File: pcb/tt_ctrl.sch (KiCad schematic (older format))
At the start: 14 parts

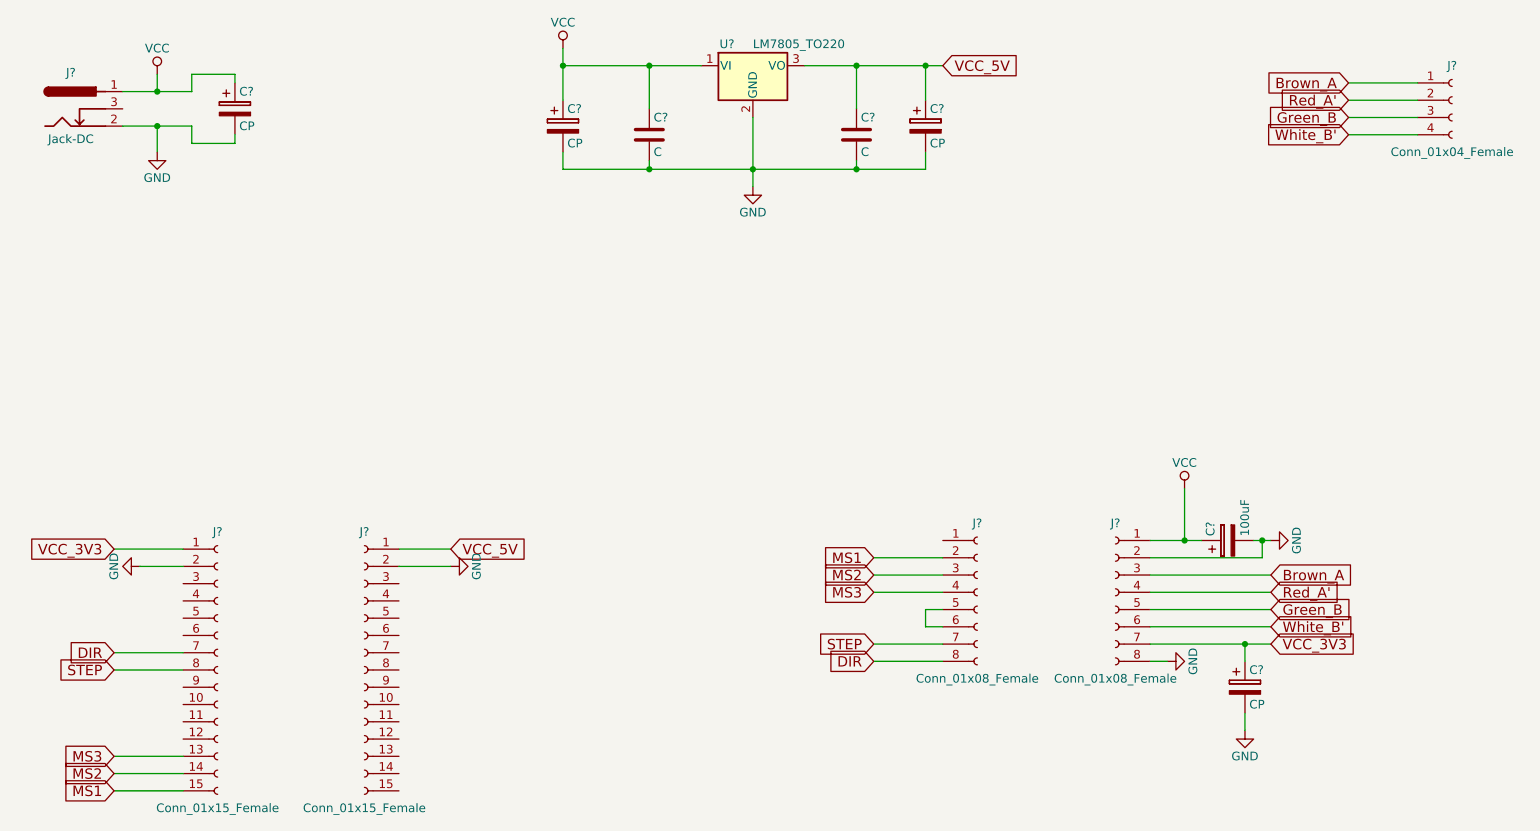
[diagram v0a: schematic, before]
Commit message: First version of the PCB added.
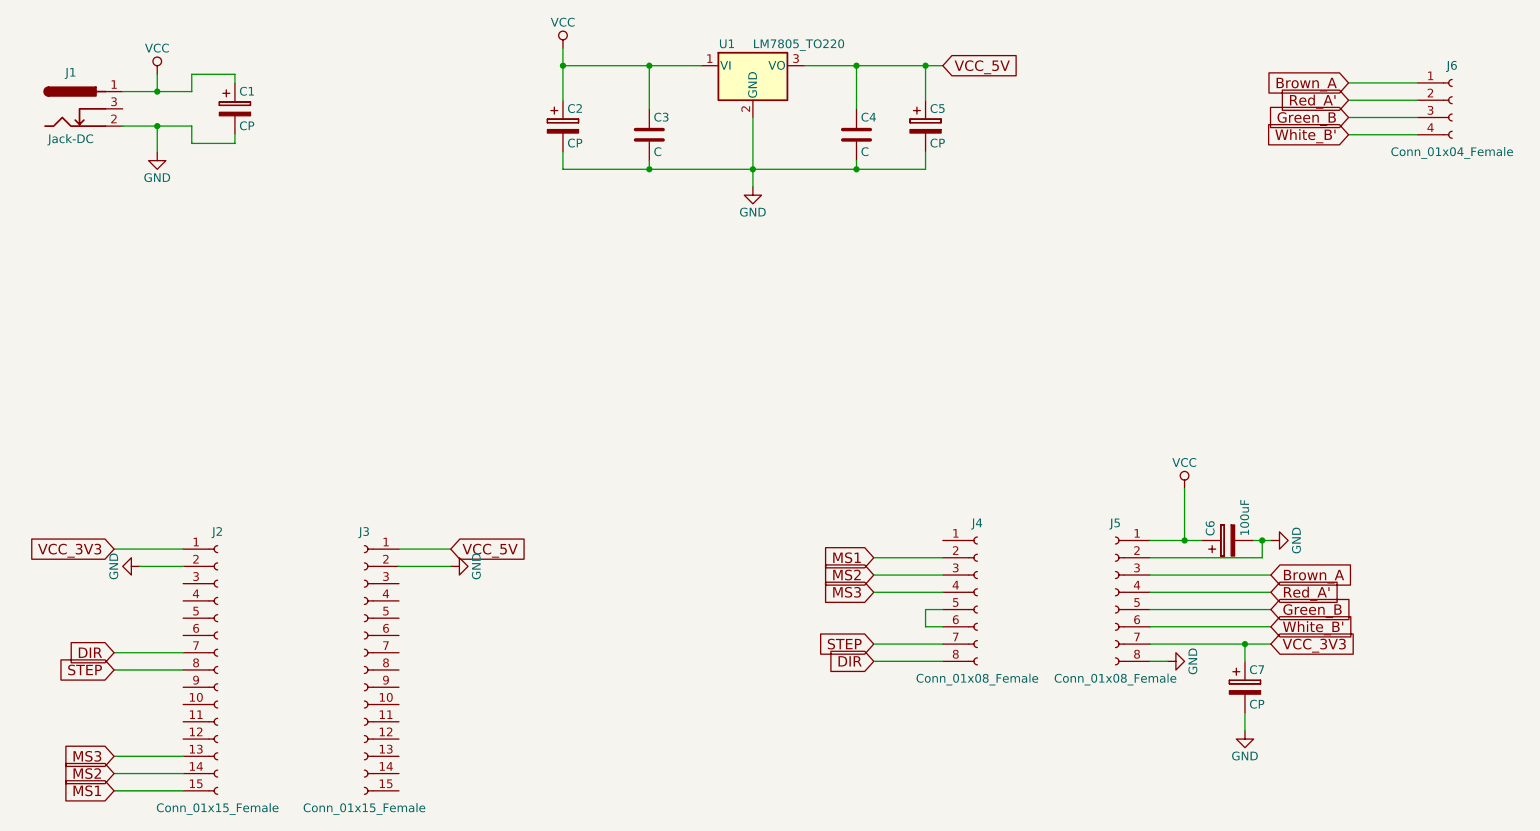
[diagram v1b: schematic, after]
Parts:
- C1, C2, C5, C6, C7: renamed from C?; footprint (none) -> Capacitors_THT:CP_Radial_D5.0mm_P2.50mm
- C3, C4: renamed from C?; footprint (none) -> Capacitors_THT:C_Disc_D5.0mm_W2.5mm_P2.50mm
- J1: renamed from J?; footprint (none) -> Connectors:BARREL_JACK
- J2, J3: renamed from J?; footprint (none) -> Socket_Strips:Socket_Strip_Straight_1x15_Pitch2.54mm
- J4, J5: renamed from J?; footprint (none) -> Socket_Strips:Socket_Strip_Straight_1x08_Pitch2.54mm
- J6: renamed from J?; footprint (none) -> Socket_Strips:Socket_Strip_Straight_1x04_Pitch2.54mm
- U1: renamed from U?; footprint TO_SOT_Packages_THT:TO-220_Vertical -> Power_Integrations:TO-220
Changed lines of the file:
@@
 LIBS:contrib
 LIBS:valves
+LIBS:tt_ctrl-cache
 EELAYER 25 0
 EELAYER END
@@
 $EndDescr
 $Comp
-L Jack-DC J?
+L Jack-DC J1
 U 1 1 5AFD7EE6
 P 2050 2000
-F 0 "J?" H 2050 2210 50  0000 C CNN
+F 0 "J1" H 2050 2210 50  0000 C CNN
 F 1 "Jack-DC" H 2050 1825 50  0000 C CNN
-F 2 "" H 2100 1960 50  0001 C CNN
+F 2 "Connectors:BARREL_JACK" H 2100 1960 50  0001 C CNN
 F 3 "" H 2100 1960 50  0001 C CNN
 	1    2050 2000
@@
 $EndComp
 $Comp
-L GND #PWR?
+L GND #PWR01
 U 1 1 5AFD7F7B
 P 2550 2250
-F 0 "#PWR?" H 2550 2000 50  0001 C CNN
+F 0 "#PWR01" H 2550 2000 50  0001 C CNN
 F 1 "GND" H 2550 2100 50  0000 C CNN
 F 2 "" H 2550 2250 50  0001 C CNN
@@
 $EndComp
 $Comp
-L VCC #PWR?
+L VCC #PWR02
 U 1 1 5AFD7F98
 P 2550 1800
-F 0 "#PWR?" H 2550 1650 50  0001 C CNN
+F 0 "#PWR02" H 2550 1650 50  0001 C CNN
 F 1 "VCC" H 2550 1950 50  0000 C CNN
 F 2 "" H 2550 1800 50  0001 C CNN
@@
 $EndComp
 $Comp
-L Conn_01x08_Female J?
+L Conn_01x08_Female J4
 U 1 1 5AFD7FB4
 P 7300 4800
-F 0 "J?" H 7300 5200 50  0000 C CNN
+F 0 "J4" H 7300 5200 50  0000 C CNN
 F 1 "Conn_01x08_Female" H 7300 4300 50  0000 C CNN
-F 2 "" H 7300 4800 50  0001 C CNN
+F 2 "Socket_Strips:Socket_Strip_Straight_1x08_Pitch2.54mm" H 7300 4800 50  0001 C CNN
 F 3 "" H 7300 4800 50  0001 C CNN
 	1    7300 4800
@@
 $EndComp
 $Comp
-L Conn_01x08_Female J?
+L Conn_01x08_Female J5
 U 1 1 5AFD8243
 P 8100 4800
-F 0 "J?" H 8100 5200 50  0000 C CNN
+F 0 "J5" H 8100 5200 50  0000 C CNN
 F 1 "Conn_01x08_Female" H 8100 4300 50  0000 C CNN
-F 2 "" H 8100 4800 50  0001 C CNN
+F 2 "Socket_Strips:Socket_Strip_Straight_1x08_Pitch2.54mm" H 8100 4800 50  0001 C CNN
 F 3 "" H 8100 4800 50  0001 C CNN
 	1    8100 4800
@@
 $EndComp
 $Comp
-L Conn_01x15_Female J?
+L Conn_01x15_Female J2
 U 1 1 5AFD8298
 P 2900 5250
-F 0 "J?" H 2900 6050 50  0000 C CNN
+F 0 "J2" H 2900 6050 50  0000 C CNN
 F 1 "Conn_01x15_Female" H 2900 4450 50  0000 C CNN
-F 2 "" H 2900 5250 50  0001 C CNN
+F 2 "Socket_Strips:Socket_Strip_Straight_1x15_Pitch2.54mm" H 2900 5250 50  0001 C CNN
 F 3 "" H 2900 5250 50  0001 C CNN
 	1    2900 5250
@@
 $EndComp
 $Comp
-L Conn_01x15_Female J?
+L Conn_01x15_Female J3
 U 1 1 5AFD837D
 P 3750 5250
-F 0 "J?" H 3750 6050 50  0000 C CNN
+F 0 "J3" H 3750 6050 50  0000 C CNN
 F 1 "Conn_01x15_Female" H 3750 4450 50  0000 C CNN
-F 2 "" H 3750 5250 50  0001 C CNN
+F 2 "Socket_Strips:Socket_Strip_Straight_1x15_Pitch2.54mm" H 3750 5250 50  0001 C CNN
 F 3 "" H 3750 5250 50  0001 C CNN
 	1    3750 5250
@@
 $EndComp
 $Comp
-L LM7805_TO220 U?
+L LM7805_TO220 U1
 U 1 1 5AFD841A
 P 6000 1750
-F 0 "U?" H 5850 1875 50  0000 C CNN
+F 0 "U1" H 5850 1875 50  0000 C CNN
 F 1 "LM7805_TO220" H 6000 1875 50  0000 L CNN
-F 2 "TO_SOT_Packages_THT:TO-220_Vertical" H 6000 1975 50  0001 C CIN
+F 2 "Power_Integrations:TO-220" H 6000 1975 50  0001 C CIN
 F 3 "" H 6000 1700 50  0001 C CNN
 	1    6000 1750
@@
 $EndComp
 $Comp
-L C C?
+L C C3
 U 1 1 5AFD84C3
 P 5400 2150
-F 0 "C?" H 5425 2250 50  0000 L CNN
+F 0 "C3" H 5425 2250 50  0000 L CNN
 F 1 "C" H 5425 2050 50  0000 L CNN
-F 2 "" H 5438 2000 50  0001 C CNN
+F 2 "Capacitors_THT:C_Disc_D5.0mm_W2.5mm_P2.50mm" H 5438 2000 50  0001 C CNN
 F 3 "" H 5400 2150 50  0001 C CNN
 	1    5400 2150
@@
 $EndComp
 $Comp
-L C C?
+L C C4
 U 1 1 5AFD85A1
 P 6600 2150
-F 0 "C?" H 6625 2250 50  0000 L CNN
+F 0 "C4" H 6625 2250 50  0000 L CNN
 F 1 "C" H 6625 2050 50  0000 L CNN
-F 2 "" H 6638 2000 50  0001 C CNN
+F 2 "Capacitors_THT:C_Disc_D5.0mm_W2.5mm_P2.50mm" H 6638 2000 50  0001 C CNN
 F 3 "" H 6600 2150 50  0001 C CNN
 	1    6600 2150
@@
 $EndComp
 $Comp
-L CP C?
+L CP C1
 U 1 1 5AFD878C
 P 3000 2000
-F 0 "C?" H 3025 2100 50  0000 L CNN
+F 0 "C1" H 3025 2100 50  0000 L CNN
 F 1 "CP" H 3025 1900 50  0000 L CNN
-F 2 "" H 3038 1850 50  0001 C CNN
+F 2 "Capacitors_THT:CP_Radial_D5.0mm_P2.50mm" H 3038 1850 50  0001 C CNN
 F 3 "" H 3000 2000 50  0001 C CNN
 	1    3000 2000
@@
 $EndComp
 $Comp
-L CP C?
+L CP C5
 U 1 1 5AFD886B
 P 7000 2100
-F 0 "C?" H 7025 2200 50  0000 L CNN
+F 0 "C5" H 7025 2200 50  0000 L CNN
 F 1 "CP" H 7025 2000 50  0000 L CNN
-F 2 "" H 7038 1950 50  0001 C CNN
+F 2 "Capacitors_THT:CP_Radial_D5.0mm_P2.50mm" H 7038 1950 50  0001 C CNN
 F 3 "" H 7000 2100 50  0001 C CNN
 	1    7000 2100
@@
 $EndComp
 $Comp
-L CP C?
+L CP C6
 U 1 1 5AFD89BB
 P 8750 4500
-F 0 "C?" H 8775 4600 50  0000 L CNN
+F 0 "C6" H 8775 4600 50  0000 L CNN
 F 1 "100uF" H 8775 4400 50  0000 L CNN
-F 2 "" H 8788 4350 50  0001 C CNN
+F 2 "Capacitors_THT:CP_Radial_D5.0mm_P2.50mm" H 8788 4350 50  0001 C CNN
 F 3 "" H 8750 4500 50  0001 C CNN
 	1    8750 4500
@@
 $EndComp
 $Comp
-L GND #PWR?
+L GND #PWR03
 U 1 1 5AFD8D7F
 P 6000 2450
-F 0 "#PWR?" H 6000 2200 50  0001 C CNN
+F 0 "#PWR03" H 6000 2200 50  0001 C CNN
 F 1 "GND" H 6000 2300 50  0000 C CNN
 F 2 "" H 6000 2450 50  0001 C CNN
@@
 $EndComp
 $Comp
-L CP C?
+L CP C2
 U 1 1 5AFD8DA6
 P 4900 2100
-F 0 "C?" H 4925 2200 50  0000 L CNN
+F 0 "C2" H 4925 2200 50  0000 L CNN
 F 1 "CP" H 4925 2000 50  0000 L CNN
-F 2 "" H 4938 1950 50  0001 C CNN
+F 2 "Capacitors_THT:CP_Radial_D5.0mm_P2.50mm" H 4938 1950 50  0001 C CNN
 F 3 "" H 4900 2100 50  0001 C CNN
 	1    4900 2100
@@
 $EndComp
 $Comp
-L Conn_01x04_Female J?
+L Conn_01x04_Female J6
 U 1 1 5AFD8E73
 P 10050 1950
-F 0 "J?" H 10050 2150 50  0000 C CNN
+F 0 "J6" H 10050 2150 50  0000 C CNN
 F 1 "Conn_01x04_Female" H 10050 1650 50  0000 C CNN
-F 2 "" H 10050 1950 50  0001 C CNN
+F 2 "Socket_Strips:Socket_Strip_Straight_1x04_Pitch2.54mm" H 10050 1950 50  0001 C CNN
 F 3 "" H 10050 1950 50  0001 C CNN
 	1    10050 1950
@@
 $EndComp
 $Comp
-L VCC #PWR?
+L VCC #PWR04
 U 1 1 5AFD947A
 P 4900 1650
-F 0 "#PWR?" H 4900 1500 50  0001 C CNN
+F 0 "#PWR04" H 4900 1500 50  0001 C CNN
 F 1 "VCC" H 4900 1800 50  0000 C CNN
 F 2 "" H 4900 1650 50  0001 C CNN
@@
 $EndComp
 $Comp
-L GND #PWR?
+L GND #PWR05
 U 1 1 5AFD97A2
 P 8850 5600
-F 0 "#PWR?" H 8850 5350 50  0001 C CNN
+F 0 "#PWR05" H 8850 5350 50  0001 C CNN
 F 1 "GND" H 8850 5450 50  0000 C CNN
 F 2 "" H 8850 5600 50  0001 C CNN
@@
 VCC_5V
 $Comp
-L GND #PWR?
+L GND #PWR06
 U 1 1 5AFD9FFE
 P 9000 4500
-F 0 "#PWR?" H 9000 4250 50  0001 C CNN
+F 0 "#PWR06" H 9000 4250 50  0001 C CNN
 F 1 "GND" H 9000 4350 50  0000 C CNN
 F 2 "" H 9000 4500 50  0001 C CNN
@@
 White_B'
 $Comp
-L VCC #PWR?
+L VCC #PWR07
 U 1 1 5AFDAC35
 P 8500 4200
-F 0 "#PWR?" H 8500 4050 50  0001 C CNN
+F 0 "#PWR07" H 8500 4050 50  0001 C CNN
 F 1 "VCC" H 8500 4350 50  0000 C CNN
 F 2 "" H 8500 4200 50  0001 C CNN
@@
 $EndComp
 $Comp
-L GND #PWR?
+L GND #PWR08
 U 1 1 5AFDB15F
 P 8400 5200
-F 0 "#PWR?" H 8400 4950 50  0001 C CNN
+F 0 "#PWR08" H 8400 4950 50  0001 C CNN
 F 1 "GND" H 8400 5050 50  0000 C CNN
 F 2 "" H 8400 5200 50  0001 C CNN
@@
 $EndComp
 $Comp
-L CP C?
+L CP C7
 U 1 1 5AFDB238
 P 8850 5350
-F 0 "C?" H 8875 5450 50  0000 L CNN
+F 0 "C7" H 8875 5450 50  0000 L CNN
 F 1 "CP" H 8875 5250 50  0000 L CNN
-F 2 "" H 8888 5200 50  0001 C CNN
+F 2 "Capacitors_THT:CP_Radial_D5.0mm_P2.50mm" H 8888 5200 50  0001 C CNN
 F 3 "" H 8850 5350 50  0001 C CNN
 	1    8850 5350
@@
 VCC_3V3
 $Comp
-L GND #PWR?
+L GND #PWR09
 U 1 1 5AFDBDB5
 P 2450 4650
-F 0 "#PWR?" H 2450 4400 50  0001 C CNN
+F 0 "#PWR09" H 2450 4400 50  0001 C CNN
 F 1 "GND" H 2450 4500 50  0000 C CNN
 F 2 "" H 2450 4650 50  0001 C CNN
@@
 VCC_5V
 $Comp
-L GND #PWR?
+L GND #PWR010
 U 1 1 5AFDC2CF
 P 4250 4650
-F 0 "#PWR?" H 4250 4400 50  0001 C CNN
+F 0 "#PWR010" H 4250 4400 50  0001 C CNN
 F 1 "GND" H 4250 4500 50  0000 C CNN
 F 2 "" H 4250 4650 50  0001 C CNN
